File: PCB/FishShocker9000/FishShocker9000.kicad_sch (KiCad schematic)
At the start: 205 parts, among them J1 Barrel_Jack, J10 P70-1000045R, J100 P70-1000045R, J101 P70-1000045R, J102 P70-1000045R, J103 P70-1000045R, J104 P70-1000045R, J105 P70-1000045R, J106 P70-1000045R, J107 P70-1000045R, J108 P70-1000045R, J109 P70-1000045R, J11 P70-1000045R, J110 P70-1000045R, J111 P70-1000045R, J112 P70-1000045R, J113 P70-1000045R, J114 P70-1000045R, J115 P70-1000045R, J116 P70-1000045R, J117 P70-1000045R, J118 P70-1000045R, J119 P70-1000045R, J12 P70-1000045R, J120 P70-1000045R, J121 P70-1000045R, J122 P70-1000045R, J123 P70-1000045R, J124 P70-1000045R, J125 P70-1000045R, J126 P70-1000045R, J127 P70-1000045R, J128 P70-1000045R, J129 P70-1000045R, J13 P70-1000045R, J130 P70-1000045R, J131 P70-1000045R, J132 P70-1000045R, J133 P70-1000045R, J134 P70-1000045R, J135 P70-1000045R, J136 P70-1000045R, J137 P70-1000045R, J138 P70-1000045R, J139 P70-1000045R, J14 P70-1000045R, J140 P70-1000045R, J141 P70-1000045R, J142 P70-1000045R, J143 P70-1000045R, J144 P70-1000045R, J145 P70-1000045R, J15 P70-1000045R, J16 P70-1000045R, J17 P70-1000045R, J18 P70-1000045R, J19 P70-1000045R, J2 P70-1000045R, J20 P70-1000045R, J21 P70-1000045R, J22 P70-1000045R, J23 P70-1000045R, J24 P70-1000045R, J25 P70-1000045R, J26 P70-1000045R, J27 P70-1000045R, J28 P70-1000045R, J29 P70-1000045R, J3 P70-1000045R, J30 P70-1000045R, J31 P70-1000045R, J32 P70-1000045R, J33 P70-1000045R, J34 P70-1000045R, J35 P70-1000045R, J36 P70-1000045R, J37 P70-1000045R, J38 P70-1000045R, J39 P70-1000045R, J4 P70-1000045R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

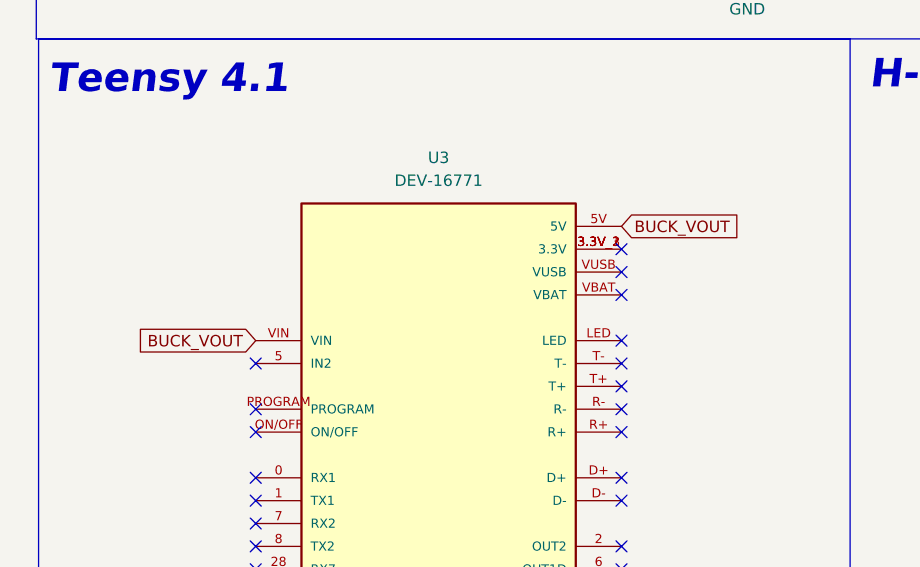
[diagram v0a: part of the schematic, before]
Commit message: Fixed Teensy being double powered
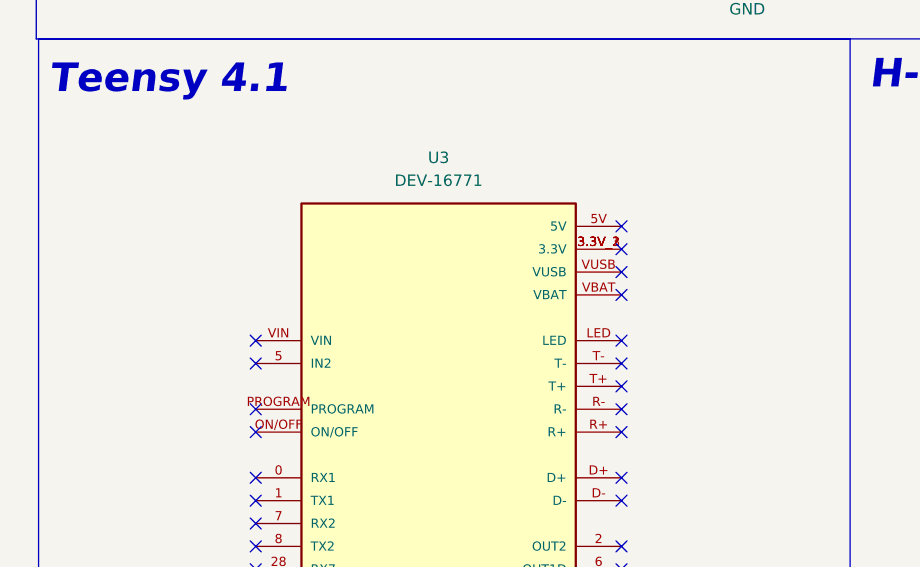
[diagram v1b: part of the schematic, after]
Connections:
- net BUCK_VOUT: no longer U3.5V, U3.VIN
- no-connect marks 37 -> 39
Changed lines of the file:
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@@
 	)
 	(no_connect
+		(at 77.47 91.44)
+	)
+	(no_connect
 		(at 36.83 137.16)
 	)
@@
 	)
 	(no_connect
+		(at 36.83 104.14)
+	)
+	(no_connect
 		(at 77.47 167.64)
 	)
@@
 		)
 	)
-	(global_label "BUCK_VOUT"
-		(shape input)
-		(at 36.83 104.14 180)
-		(fields_autoplaced yes)
-		(effects
-			(font
-				(size 1.27 1.27)
-			)
-			(justify right)
-		)
-		(property "Intersheetrefs" "${INTERSHEET_REFS}"
-			(at 23.0195 104.14 0)
-			(effects
-				(font
-					(size 1.27 1.27)
-				)
-				(justify right)
-				(hide yes)
-			)
-		)
-	)
 	(global_label "BUCK_PG"
 		(shape input)
@@
 				(hide yes)
 			)
-		)
-	)
-	(global_label "BUCK_VOUT"
-		(shape input)
-		(at 77.47 91.44 0)
-		(fields_autoplaced yes)
-		(effects
-			(font
-				(size 1.27 1.27)
-			)
-			(justify left)
-		)
-		(property "Intersheetrefs" "${INTERSHEET_REFS}"
-			(at 91.2805 91.44 0)
-			(effects
-				(font
-					(size 1.27 1.27)
-				)
-				(justify left)
-				(hide yes)
-			)

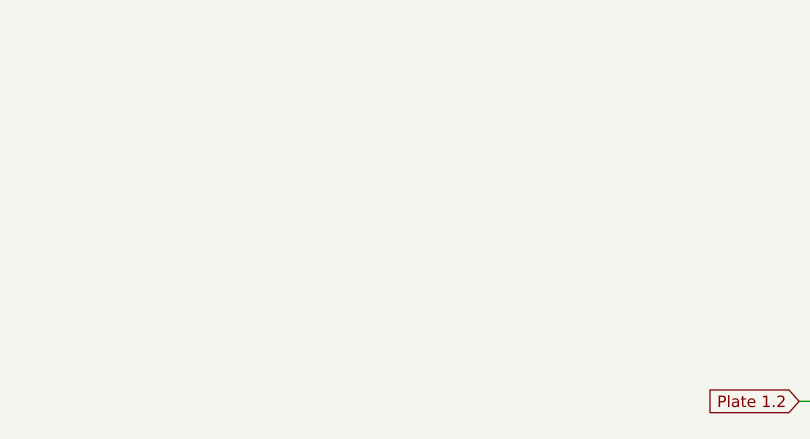
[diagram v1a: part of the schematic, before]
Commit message: Added testing headers
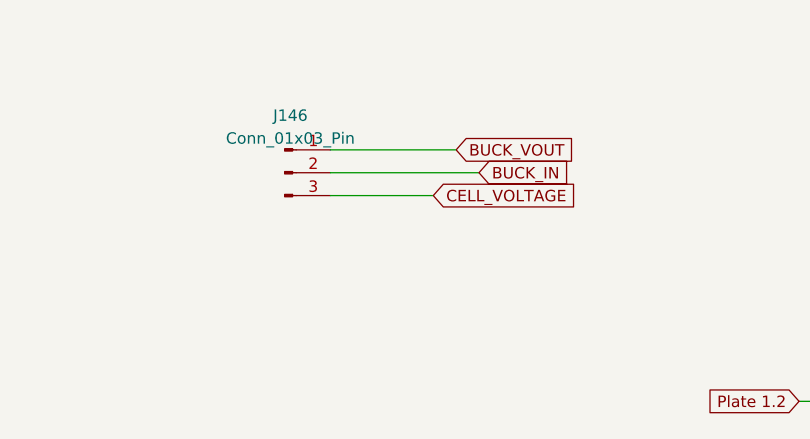
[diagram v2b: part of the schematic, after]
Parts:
- added J146: Conn_01x03_Pin, Connector_PinHeader_1.00mm:PinHeader_1x03_P1.00mm_Horizontal, symbol Connector:Conn_01x03_Pin
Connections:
- net BUCK_IN: now also J146.2 (Pin_2)
- net BUCK_VOUT: now also J146.1 (Pin_1)
- net CELL_VOLTAGE: now also J146.3 (Pin_3)
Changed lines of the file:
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@@
 	(wire
 		(pts
+			(xy 406.4 -19.05) (xy 389.89 -19.05)
+		)
+		(stroke
+			(width 0)
+			(type default)
+		)
+	)
+	(wire
+		(pts
 			(xy 346.71 44.45) (xy 351.79 44.45)
 		)
@@
 	(wire
 		(pts
+			(xy 389.89 -21.59) (xy 403.86 -21.59)
+		)
+		(stroke
+			(width 0)
+			(type default)
+		)
+	)
+	(wire
+		(pts
 			(xy 153.67 109.22) (xy 156.21 109.22)
 		)
@@
 	(wire
 		(pts
+			(xy 401.32 -16.51) (xy 389.89 -16.51)
+		)
+		(stroke
+			(width 0)
+			(type default)
+		)
+	)
+	(wire
+		(pts
 			(xy 464.82 184.15) (xy 464.82 182.88)
 		)
@@
 		)
 	)
+	(global_label "BUCK_VOUT"
+		(shape input)
+		(at 403.86 -21.59 0)
+		(fields_autoplaced yes)
+		(effects
+			(font
+				(size 1.27 1.27)
+			)
+			(justify left)
+		)
+		(property "Intersheetrefs" "${INTERSHEET_REFS}"
+			(at 417.6705 -21.59 0)
+			(effects
+				(font
+					(size 1.27 1.27)
+				)
+				(justify left)
+				(hide yes)
+			)
+		)
+	)
 	(global_label "CELL_2"
 		(shape input)
@@
 		)
 	)
+	(global_label "CELL_VOLTAGE"
+		(shape input)
+		(at 401.32 -16.51 0)
+		(fields_autoplaced yes)
+		(effects
+			(font
+				(size 1.27 1.27)
+			)
+			(justify left)
+		)
+		(property "Intersheetrefs" "${INTERSHEET_REFS}"
+			(at 417.6704 -16.51 0)
+			(effects
+				(font
+					(size 1.27 1.27)
+				)
+				(justify left)
+				(hide yes)
+			)
+		)
+	)
 	(global_label "Polarity Enable 1"
 		(shape input)
@@
 		)
 	)
+	(global_label "BUCK_IN"
+		(shape input)
+		(at 406.4 -19.05 0)
+		(fields_autoplaced yes)
+		(effects
+			(font
+				(size 1.27 1.27)
+			)
+			(justify left)
+		)
+		(property "Intersheetrefs" "${INTERSHEET_REFS}"
+			(at 417.4286 -19.05 0)
+			(effects
+				(font
+					(size 1.27 1.27)
+				)
+				(justify left)
+				(hide yes)
+			)
+		)
+	)
 	(global_label "CELL_10"
 		(shape input)
@@
 					(unit 1)
 				)
+			)
+		)
+	)
+	(symbol
+		(lib_id "Connector:Conn_01x03_Pin")
+		(at 384.81 -19.05 0)
+		(unit 1)
+		(exclude_from_sim no)
+		(in_bom yes)
+		(on_board yes)
+		(dnp no)
+		(fields_autoplaced yes)
+		(property "Reference" "J146"
+			(at 385.445 -25.4 0)
+			(effects
+				(font
+					(size 1.27 1.27)
+				)
+			)
+		)
+		(property "Value" "Conn_01x03_Pin"
+			(at 385.445 -22.86 0)
+			(effects
+				(font
+					(size 1.27 1.27)
+				)
+			)
+		)
+		(property "Footprint" "Connector_PinHeader_1.00mm:PinHeader_1x03_P1.00mm_Horizontal"
+			(at 384.81 -19.05 0)
+			(effects
+				(font
+					(size 1.27 1.27)
+				)
+				(hide yes)
+			)
+		)
+		(property "Datasheet" "~"
+			(at 384.81 -19.05 0)
+			(effects
+				(font
+					(size 1.27 1.27)
+				)
+				(hide yes)
+			)
+		)
+		(property "Description" "Generic connector, single row, 01x03, script generated"
+			(at 384.81 -19.05 0)
+			(effects
+				(font
+					(size 1.27 1.27)
+				)
+				(hide yes)
+			)
+		)
+		(pin "1"
+		)
+		(pin "2"
+		)
+		(pin "3"
+		)
+		(instances
+			(project ""
+				(path "/1c185f74-5dfc-4a92-a3ad-4e1ef719d398"
+					(reference "J146")
+					(unit 1)
+				)

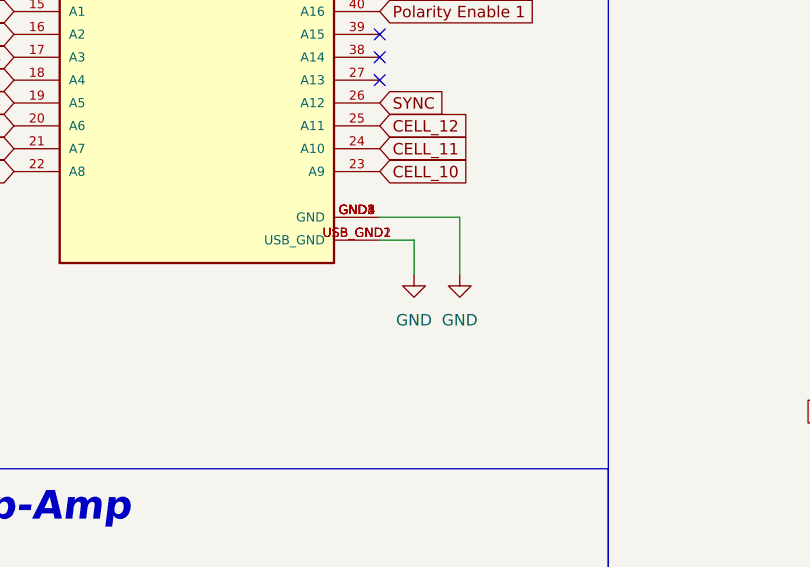
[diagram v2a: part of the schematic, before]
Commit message: removed USB gnd
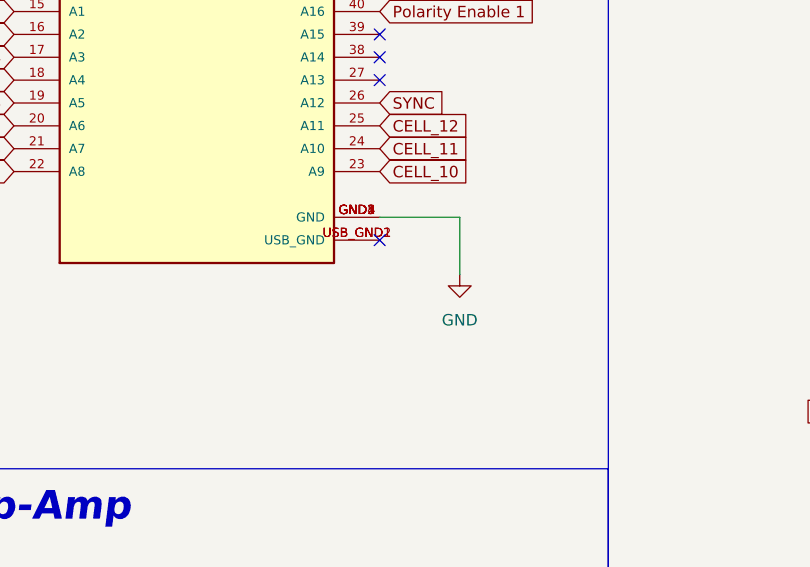
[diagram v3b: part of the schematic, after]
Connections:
- net GND: no longer U3.USB_GND1 (USB_GND), U3.USB_GND2 (USB_GND)
- new net: U3.USB_GND1 (USB_GND), U3.USB_GND2 (USB_GND)
- no-connect marks 39 -> 40
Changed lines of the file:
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@@
 	)
 	(no_connect
+		(at 77.47 187.96)
+	)
+	(no_connect
 		(at 77.47 121.92)
 	)
@@
 	(wire
 		(pts
-			(xy 77.47 187.96) (xy 81.28 187.96)
-		)
-		(stroke
-			(width 0)
-			(type default)
-		)
-	)
-	(wire
-		(pts
 			(xy 709.93 227.33) (xy 740.41 227.33)
 		)
@@
 	(wire
 		(pts
-			(xy 81.28 187.96) (xy 81.28 191.77)
-		)
-		(stroke
-			(width 0)
-			(type default)
-		)
-	)
-	(wire
-		(pts
 			(xy 774.7 172.72) (xy 774.7 171.45)
 		)
@@
 					(unit 1)
 				)
-			)
-		)
-	)
-	(symbol
-		(lib_id "power:GND")
-		(at 81.28 191.77 0)
-		(unit 1)
-		(exclude_from_sim no)
-		(in_bom yes)
-		(on_board yes)
-		(dnp no)
-		(fields_autoplaced yes)
-		(property "Reference" "#PWR061"
-			(at 81.28 198.12 0)
-			(effects
-				(font
-					(size 1.27 1.27)
-				)
-				(hide yes)
-			)
-		)
-		(property "Value" "GND"
-			(at 81.28 196.85 0)
-			(effects
-				(font
-					(size 1.27 1.27)
-				)
-			)
-		)
-		(property "Footprint" ""
-			(at 81.28 191.77 0)
-			(effects
-				(font
-					(size 1.27 1.27)
-				)
-				(hide yes)
-			)
-		)
-		(property "Datasheet" ""
-			(at 81.28 191.77 0)
-			(effects
-				(font
-					(size 1.27 1.27)
-				)
-				(hide yes)
-			)
-		)
-		(property "Description" "Power symbol creates a global label with name \"GND\" , ground"
-			(at 81.28 191.77 0)
-			(effects
-				(font
-					(size 1.27 1.27)
-				)
-				(hide yes)
-			)
-		)
-		(pin "1"
-		)
-		(instances
-			(project "FishShocker9000"
-				(path "/1c185f74-5dfc-4a92-a3ad-4e1ef719d398"
-					(reference "#PWR061")
-					(unit 1)
-				)

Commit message: Fixed more corruption
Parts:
- J146: footprint Connector_PinHeader_1.00mm:PinHeader_1x03_P1.00mm_Horizontal -> Connector_PinHeader_1.00mm:PinHeader_1x03_P1.00mm_Vertical
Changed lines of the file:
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@@
 			)
 		)
-		(property "Footprint" "Connector_PinHeader_1.00mm:PinHeader_1x03_P1.00mm_Horizontal"
+		(property "Footprint" "Connector_PinHeader_1.00mm:PinHeader_1x03_P1.00mm_Vertical"
 			(at 384.81 -19.05 0)
 			(effects

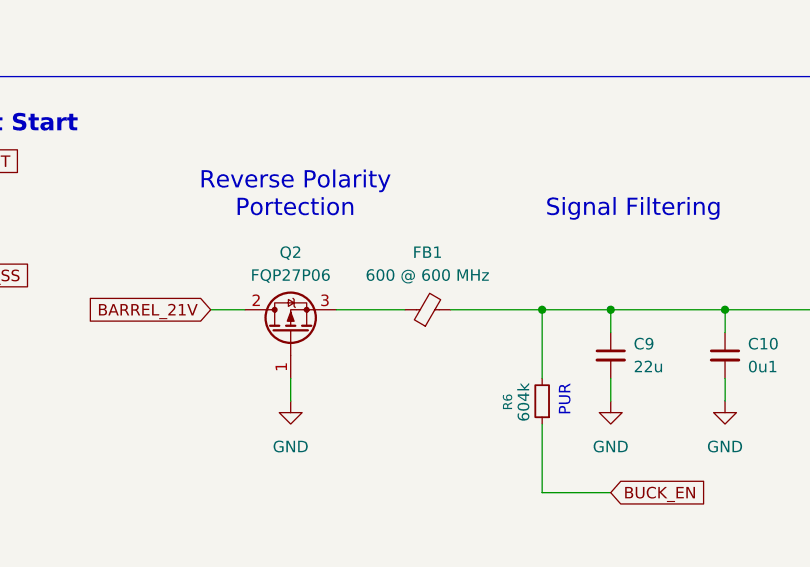
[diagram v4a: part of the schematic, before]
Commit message: Changed pogo pin footprints to connector, fixed routing, removed ferrite bead
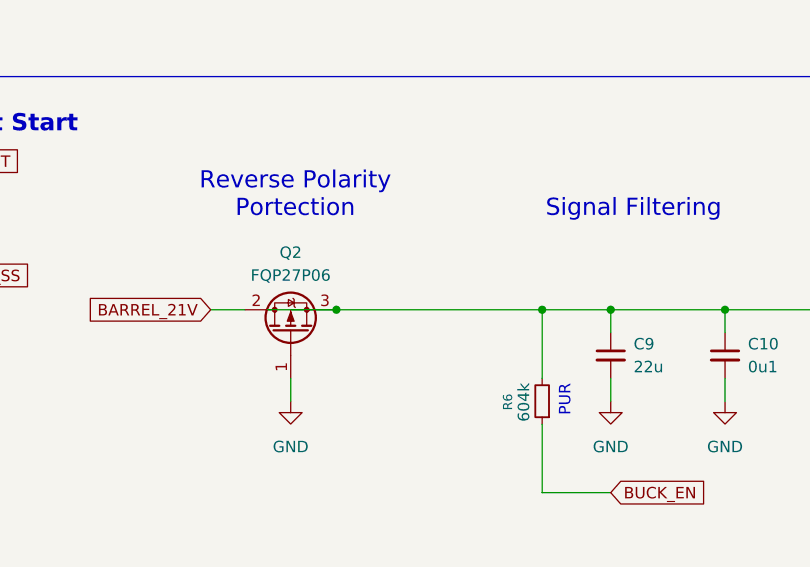
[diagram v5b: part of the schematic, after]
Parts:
- removed FB1: 600 @ 600 MHz, Inductor_SMD:L_0805_2012Metric, symbol Device:FerriteBead_Small
- J10, J100, J101, J102, J103, J104, J105, J106, J107, J108, J109, J11, J110, J111, J112, J113, J114, J115, J116, J117, J118, J119, J12, J120, J121, J122, J123, J124, J125, J126, J127, J128, J129, J13, J130, J131, J132, J133, J134, J135, J136, J137, J138, J139, J14, J140, J141, J142, J143, J144, J145, J15, J16, J17, J18, J19, J2, J20, J21, J22, J23, J24, J25, J26, J27, J28, J29, J3, J30, J31, J32, J33, J34, J35, J36, J37, J38, J39, J4, J40, J41, J42, J43, J44, J45, J46, J47, J48, J49, J5, J50, J51, J52, J53, J54, J55, J56, J57, J58, J59, J6, J60, J61, J62, J63, J64, J65, J66, J67, J68, J69, J7, J70, J71, J72, J73, J74, J75, J76, J77, J78, J79, J8, J80, J81, J82, J83, J84, J85, J86, J87, J88, J89, J9, J90, J91, J92, J93, J94, J95, J96, J97, J98, J99: footprint Library:HARWIN_P70-1000045R -> Connector_PinHeader_2.54mm:PinHeader_1x01_P2.54mm_Vertical
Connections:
- net BUCK_IN: now also Q2.3 (S)
